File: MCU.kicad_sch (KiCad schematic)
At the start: 12 parts, among them SW301 RESET, U202 NUCLEO64-H503RB

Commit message: Changed two connectors
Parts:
- U202: footprint ProjectConnectors:Nucleo64 -> ProjectConnectors:Nucleo64_ST-Morpho
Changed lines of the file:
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@@
 			)
 		)
-		(property "Footprint" "ProjectConnectors:Nucleo64"
+		(property "Footprint" "ProjectConnectors:Nucleo64_ST-Morpho"
 			(at 65.532 128.778 0)
 			(effects

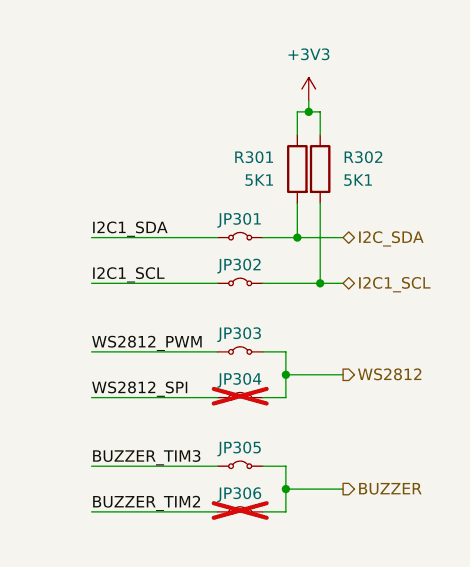
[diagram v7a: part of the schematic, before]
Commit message: Started the floorplan + added the Power LED
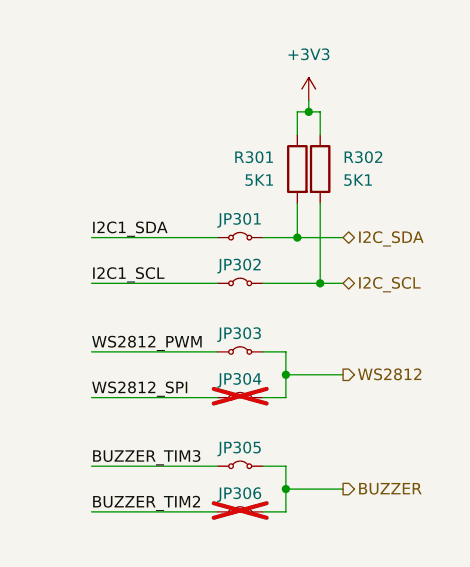
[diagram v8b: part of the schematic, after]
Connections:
- net I2C1_SCL: no longer JP302.2 (B), R302.2
- new net I2C_SCL: JP302.2 (B), R302.2
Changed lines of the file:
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@@
 		)
 	)
-	(hierarchical_label "I2C1_SCL"
+	(hierarchical_label "I2C_SCL"
 		(shape bidirectional)
 		(at 234.95 53.34 0)
